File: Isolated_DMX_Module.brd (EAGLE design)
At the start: 40 x 20 mm, 22 parts, among them IC1 75176AD, U1 TLP2362(TPL,E(T, U2 TLP2362(TPL,E(T, U3 TLP2362(TPL,E(T

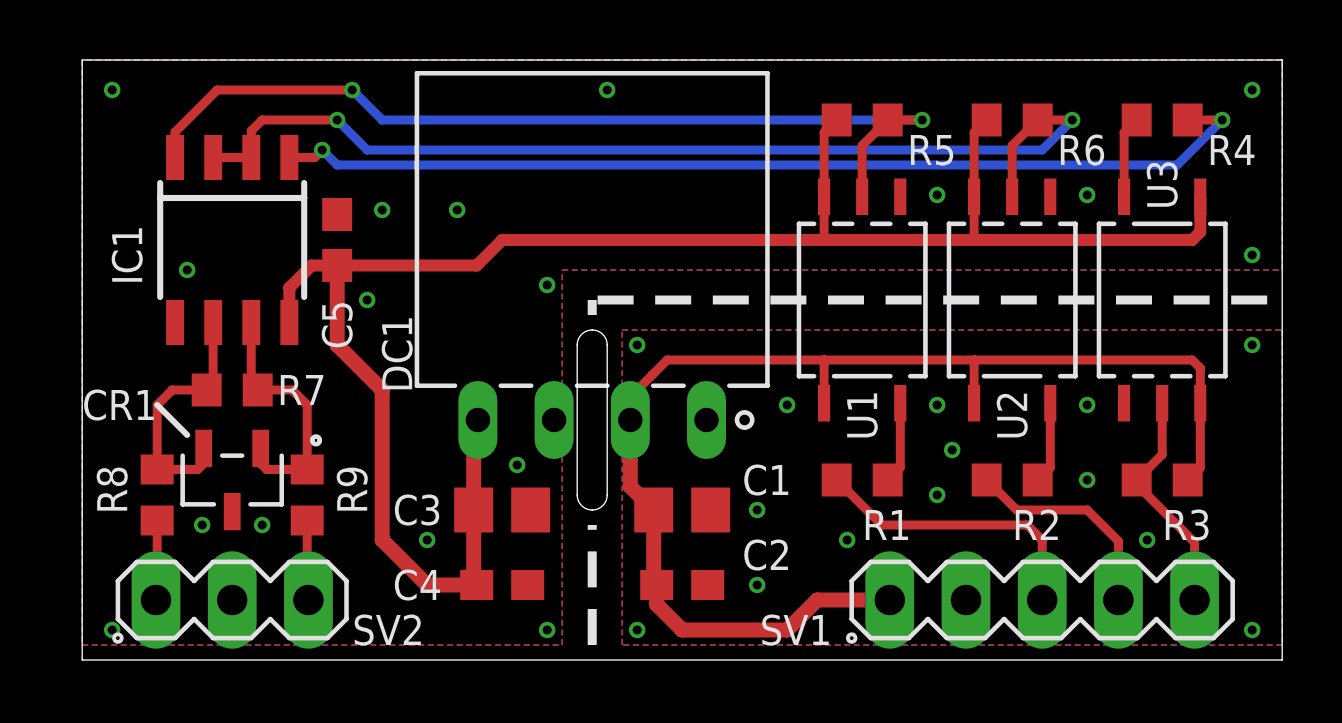
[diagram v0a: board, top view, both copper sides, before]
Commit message: Updated spacing between pin headers to be within a 0.1" grid - This way it is breadboard compatible
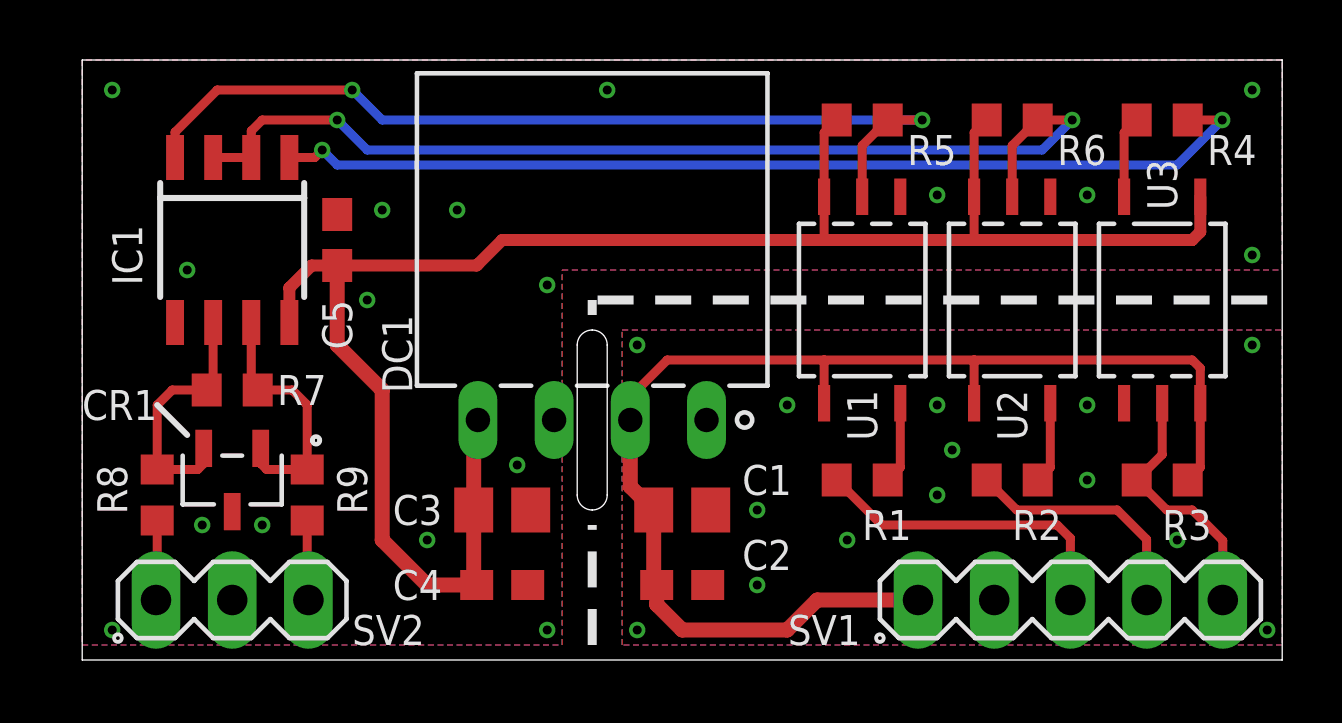
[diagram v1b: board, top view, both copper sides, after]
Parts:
- moved SV1 0.94 mm to (32.9, 2.00)
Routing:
- net TXD: track 7.71 -> 8.75 mm
- net DIR: track 7.19 -> 8.17 mm
- net RXD: track 9.68 -> 10.7 mm
- net VCC: track 42.2 -> 43.2 mm
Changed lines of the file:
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@@
 <attribute name="VALUE" x="1.19" y="-0.921" size="1.27" layer="27" ratio="10"/>
 </element>
-<element name="SV1" library="con-lstb" library_urn="urn:adsk.eagle:library:41989194" package="MA05-1" package3d_urn="urn:adsk.eagle:package:41989206/1" value="" x="32" y="2" smashed="yes">
-<attribute name="MF" value="" x="52.32" y="-14.51" size="1.778" layer="27" display="off"/>
-<attribute name="MPN" value="" x="52.32" y="-14.51" size="1.778" layer="27" display="off"/>
-<attribute name="NAME" x="25" y="1" size="1" layer="25" font="vector" ratio="13" rot="R180" align="center-left"/>
-<attribute name="OC_FARNELL" value="unknown" x="52.32" y="-14.51" size="1.778" layer="27" display="off"/>
-<attribute name="OC_NEWARK" value="unknown" x="52.32" y="-14.51" size="1.778" layer="27" display="off"/>
-<attribute name="POPULARITY" value="29" x="52.32" y="-14.51" size="1.778" layer="27" display="off"/>
-<attribute name="VALUE" x="29.46" y="-0.921" size="1.27" layer="27" ratio="10"/>
+<element name="SV1" library="con-lstb" library_urn="urn:adsk.eagle:library:41989194" package="MA05-1" package3d_urn="urn:adsk.eagle:package:41989206/1" value="" x="32.94" y="2" smashed="yes">
+<attribute name="MF" value="" x="53.26" y="-14.51" size="1.778" layer="27" display="off"/>
+<attribute name="MPN" value="" x="53.26" y="-14.51" size="1.778" layer="27" display="off"/>
+<attribute name="NAME" x="25.94" y="1" size="1" layer="25" font="vector" ratio="13" rot="R180" align="center-left"/>
+<attribute name="OC_FARNELL" value="unknown" x="53.26" y="-14.51" size="1.778" layer="27" display="off"/>
+<attribute name="OC_NEWARK" value="unknown" x="53.26" y="-14.51" size="1.778" layer="27" display="off"/>
+<attribute name="POPULARITY" value="29" x="53.26" y="-14.51" size="1.778" layer="27" display="off"/>
+<attribute name="VALUE" x="30.4" y="-0.921" size="1.27" layer="27" ratio="10"/>
 </element>
 <element name="U1" library="Eigene-Rietig" library_urn="urn:adsk.eagle:library:40964436" package="11-4L1S_TOS" package3d_urn="urn:adsk.eagle:package:45215040/2" value="TLP2362(TPL,E(T" x="26" y="12" smashed="yes" rot="R90">
@@
 </polygon>
 <via x="39" y="10.5" extent="1-16" drill="0.3"/>
-<via x="39" y="1" extent="1-16" drill="0.3"/>
+<via x="39.5" y="1" extent="1-16" drill="0.3"/>
 <via x="18.5" y="1" extent="1-16" drill="0.3"/>
 <via x="18.5" y="10.5" extent="1-16" drill="0.3"/>
@@
 <via x="28.5" y="5.5" extent="1-16" drill="0.3"/>
 <via x="33.5" y="6" extent="1-16" drill="0.3"/>
-<via x="35.5" y="4" extent="1-16" drill="0.3"/>
+<via x="36.5" y="4" extent="1-16" drill="0.3"/>
 <via x="25.5" y="4" extent="1-16" drill="0.3"/>
 <via x="29" y="7" extent="1-16" drill="0.3"/>
@@
 <contactref element="C2" pad="1"/>
 <contactref element="C1" pad="1"/>
-<wire x1="26.92" y1="2" x2="24.5" y2="2" width="0.5" layer="1"/>
+<wire x1="27.86" y1="2" x2="24.5" y2="2" width="0.5" layer="1"/>
 <wire x1="24.5" y1="2" x2="23.5" y2="1" width="0.5" layer="1"/>
 <wire x1="23.5" y1="1" x2="20" y2="1" width="0.5" layer="1"/>
@@
 <wire x1="18.27" y1="5.78" x2="18.27" y2="8" width="0.5" layer="1"/>
 <wire x1="18.27" y1="8" x2="18.27" y2="8.77" width="0.4" layer="1"/>
-<wire x1="18.27" y1="8.77" x2="19" y2="9.5" width="0.3" layer="1"/>
-<wire x1="19" y1="9.5" x2="19.5" y2="10" width="0.3" layer="1"/>
+<wire x1="18.27" y1="8.77" x2="19.5" y2="10" width="0.3" layer="1"/>
 <wire x1="19.5" y1="10" x2="24.73" y2="10" width="0.3" layer="1"/>
 </signal>
@@
 <contactref element="SV1" pad="3"/>
 <contactref element="R1" pad="1"/>
-<wire x1="32" y1="2" x2="32" y2="4" width="0.3" layer="1"/>
-<wire x1="32" y1="4" x2="31.5" y2="4.5" width="0.3" layer="1"/>
-<wire x1="31.5" y1="4.5" x2="26.65" y2="4.5" width="0.3" layer="1"/>
 <wire x1="26.65" y1="4.5" x2="25.15" y2="6" width="0.3" layer="1"/>
+<wire x1="32.94" y1="2" x2="32.94" y2="4.06" width="0.3" layer="1"/>
+<wire x1="32.94" y1="4.06" x2="32.5" y2="4.5" width="0.3" layer="1"/>
+<wire x1="32.5" y1="4.5" x2="26.65" y2="4.5" width="0.3" layer="1"/>
 </signal>
 <signal name="DIR">
 <contactref element="SV1" pad="4"/>
 <contactref element="R2" pad="1"/>
-<wire x1="34.54" y1="2" x2="34.54" y2="3.96" width="0.3" layer="1"/>
-<wire x1="34.54" y1="3.96" x2="33.5" y2="5" width="0.3" layer="1"/>
-<wire x1="33.5" y1="5" x2="31.15" y2="5" width="0.3" layer="1"/>
 <wire x1="31.15" y1="5" x2="30.15" y2="6" width="0.3" layer="1"/>
+<wire x1="35.48" y1="2" x2="35.48" y2="4.02" width="0.3" layer="1"/>
+<wire x1="35.48" y1="4.02" x2="34.5" y2="5" width="0.3" layer="1"/>
+<wire x1="34.5" y1="5" x2="31.15" y2="5" width="0.3" layer="1"/>
 </signal>
 <signal name="TXD">
@@
 <wire x1="36" y1="8.5583" x2="36" y2="6.85" width="0.3" layer="1"/>
 <wire x1="36" y1="6.85" x2="35.15" y2="6" width="0.3" layer="1"/>
-<wire x1="37.08" y1="2" x2="37.08" y2="3.92" width="0.3" layer="1"/>
 <wire x1="35.15" y1="5.85" x2="35.15" y2="6" width="0.3" layer="1"/>
-<wire x1="37.08" y1="3.92" x2="35.15" y2="5.85" width="0.3" layer="1"/>
+<wire x1="35.15" y1="6" x2="36.15" y2="5" width="0.3" layer="1"/>
+<wire x1="36.15" y1="5" x2="37" y2="5" width="0.3" layer="1"/>
+<wire x1="38.02" y1="3.98" x2="38.02" y2="2" width="0.3" layer="1"/>
+<wire x1="37" y1="5" x2="38.02" y2="3.98" width="0.3" layer="1"/>
 </signal>
 <signal name="N$5">
